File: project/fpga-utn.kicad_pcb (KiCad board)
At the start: 2 copper layers, 100 x 75 mm, 145 parts, among them J1 USB_C_Receptacle_USB2.0_16P, P1 Conector SMD 2x10, P2 Conector SMD 2x10, P3 Conector SMD 2x10, P4 Conector SMD 2x10, SW1 SW_Push, SW2 SW_Push, SW3 SW_Push, SW4 SW_Push, SW5 SW_Push, SW6 SW_Push, SW7 SW_Push, SW8 SW_Push, U1 LD1117S33TR_SOT223, U2 LD1117S12TR_SOT223, U3 USBLC6-2SC6, U4 FT2232HL, U5 M93C66, U6 ICE40HX4K-TQ144, U7 W25X40CLSN, Y1 ECS-3225MV-120-CN-TR, Y2 ECS-3225MVQ-1000-CN-TR

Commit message: pcbv1 silkscreen back connectors
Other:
- board text added: "+3V3"
- board text added: "+5V"
- board text added: "GND"
- board text added: "IOL_10A"
- board text added: "IOL_10B"
- board text added: "IOL_12A"
- board text added: "IOL_12B"
- board text added: "IOL_13A"
- board text added: "IOL_13B"
- board text added: "IOL_14A"
- board text added: "IOL_14B"
- board text added: "IOL_17A"
- board text added: "IOL_17B"
- board text added: "IOL_18A"
- board text added: "IOL_18B"
- board text added: "IOL_23A"
- board text added: "IOL_23B"
- board text added: "IOL_24A"
- board text added: "IOL_24B"
- board text added: "IOL_25A"
- board text added: "IOL_25B"
- board text added: "IOL_2A"
- board text added: "IOL_2B"
- board text added: "IOL_3A"
- board text added: "IOL_3B"
- board text added: "IOL_4A"
- board text added: "IOL_4B"
- board text added: "IOL_5A"
- board text added: "IOL_5B"
- board text added: "IOL_8A"
- board text added: "IOL_8B"
- board text added: "IOR_109"
- board text added: "IOR_110"
- board text added: "IOR_111"
- board text added: "IOR_112"
- board text added: "IOR_114"
- board text added: "IOR_115"
- board text added: "IOR_116"
- board text added: "IOR_117"
- board text added: "IOR_118"
- board text added: "IOR_119"
- board text added: "IOR_120"
- board text added: "IOR_128"
- board text added: "IOR_136"
- board text added: "IOR_137"
- board text added: "IOR_139"
- board text added: "IOR_140"
- board text added: "IOR_141"
- board text added: "IOR_144"
- board text added: "IOR_146"
- board text added: "IOR_147"
- board text added: "IOR_148"
- board text added: "IOR_152"
- board text added: "IOR_160"
- board text added: "IOR_161"
- board text added: "IOR_164"
- board text added: "IOR_165"
- board text added: "IOR_166"
- board text added: "IOR_167"

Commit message: Back silkscreen finished
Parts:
- added REF**: WEEE-Logo_4.2x6mm_SilkScreen, Symbol:WEEE-Logo_4.2x6mm_SilkScreen, B.Cu at (221.0, 145.0)
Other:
- board text added: "AZUKAR - FPGA OpenSource"
- board text added: "OSHWA UID: Pending"
- board text added: "VERSION 1.1 © 2026"
- board text added: "www.azukar.com.ar"

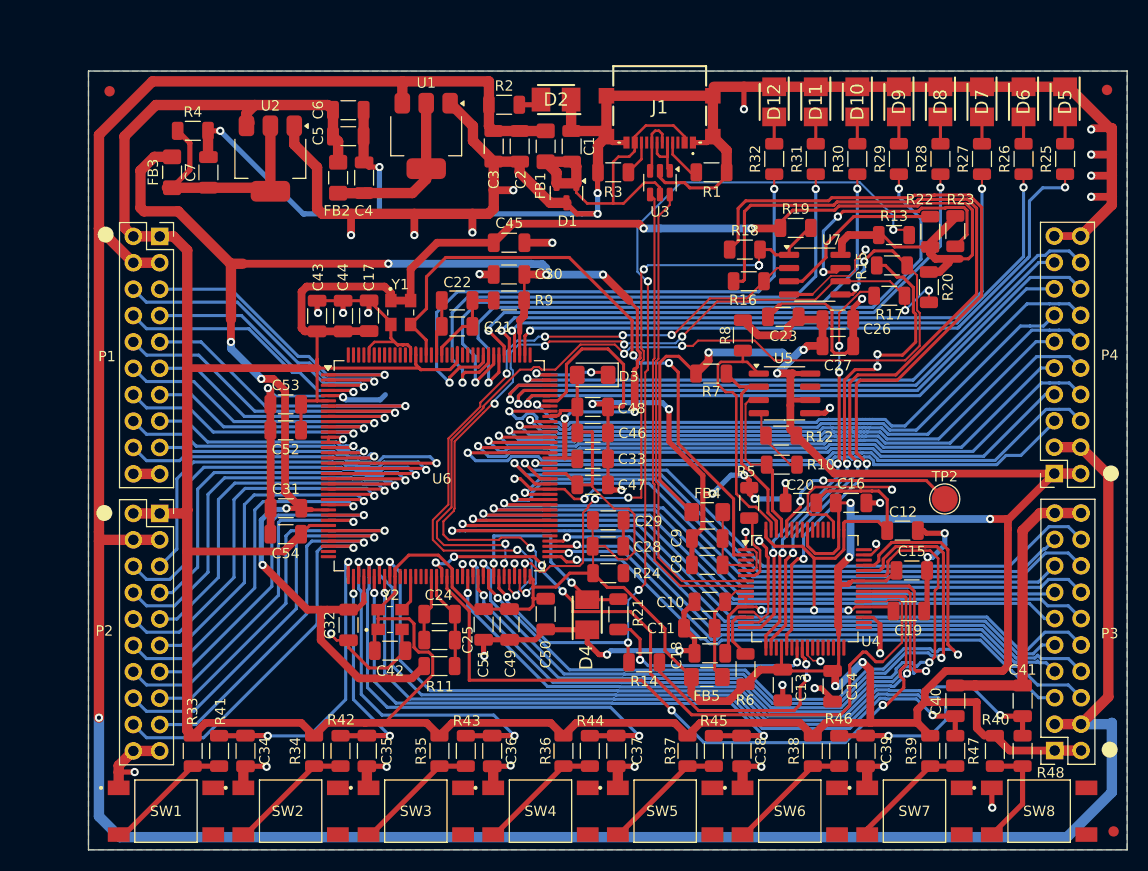
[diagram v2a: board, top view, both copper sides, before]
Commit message: pcbv1 version finalizada, correcciones de pistas, agregado logo azukar, etc
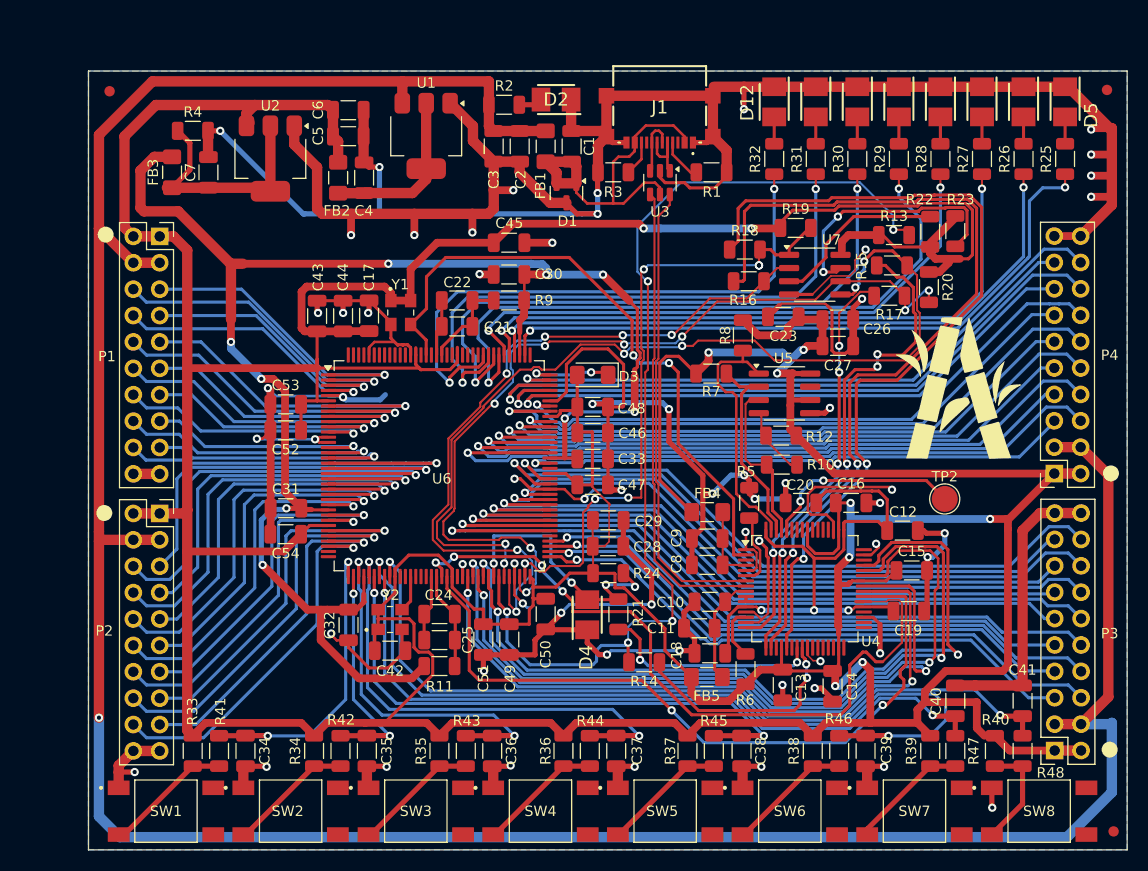
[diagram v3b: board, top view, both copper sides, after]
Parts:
- moved REF** 89.2 mm to (131.8, 145.2)
- moved C49 1.45 mm to (167.0, 129.0)
- moved C51 1.45 mm to (164.5, 129.0)
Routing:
- net GND: track 559.2 -> 592.0 mm, vias 58 -> 62
- net Net-(U6E-~{CRESET}): track 90.1 -> 99.1 mm
- net Net-(D4-A): track 20.0 -> 26.8 mm, vias 2 -> 4
- net Net-(U6E-IOB_106_SDI): track 68.1 -> 71.2 mm
- net /Perifericos/VUART_RTS: track 62.9 -> 65.4 mm
- net /Perifericos/VUART_DSR: track 74.3 -> 76.7 mm
- net /Perifericos/VUART_DCD: track 73.3 -> 75.4 mm
- net +3V3: track 669.2 -> 667.2 mm
- net /Perifericos/VUART_DTR: track 70.8 -> 72.4 mm
- net Net-(P4-IO1): track 54.8 -> 53.3 mm
- net Net-(P3-IO6): track 74.2 -> 72.8 mm
- net /Perifericos/VUART_CTS: track 68.5 -> 69.8 mm
- net Net-(P4-IO9): track 62.8 -> 62.0 mm
- net Net-(P4-IO2): track 70.9 -> 70.1 mm
- net Net-(P2-IO1): track 44.0 -> 43.1 mm
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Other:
- board text added: "AZUKAR - FPGA Tucumana"
- board text added: "BOT 1"
- board text added: "BOT 2"
- board text added: "BOT 3"
- board text added: "BOT 4"
- board text added: "BOT 5"
- board text added: "BOT 6"
- board text added: "BOT 7"
- board text added: "BOT 8"
- board text added: "IOB_56"
- board text added: "IOB_57"
- board text added: "IOB_61"
- board text added: "IOB_63"
- board text added: "IOB_64"
- board text added: "IOB_71"
- board text added: "IOB_72"
- board text added: "IOB_73"
- board text added: "IOT_168"
- board text added: "IOT_169"
- board text added: "IOT_170"
- board text added: "IOT_171"
- board text added: "IOT_172"
- board text added: "IOT_173"
- board text added: "IOT_174"
- board text added: "IOT_177"
- board text added: "LED 1"
- board text added: "LED 2"
- board text added: "LED 3"
- board text added: "LED 4"
- board text added: "LED 5"
- board text added: "LED 6"
- board text added: "LED 7"
- board text added: "LED 8"
- board text added: "ZUKAR"
- board text added: "ZUKAR - FPGA Tucumana"
- board text removed: "AZUKAR - FPGA OpenSource"

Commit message: Correccion en nombre y logo
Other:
- board text added: "AZUKAR FPGA"
- board text added: "VERSION 1.2 © 2026"
- board text removed: "AZUKAR - FPGA Tucumana"
- board text removed: "VERSION 1.1 © 2026"
- board text removed: "ZUKAR"
- board text removed: "ZUKAR - FPGA Tucumana"

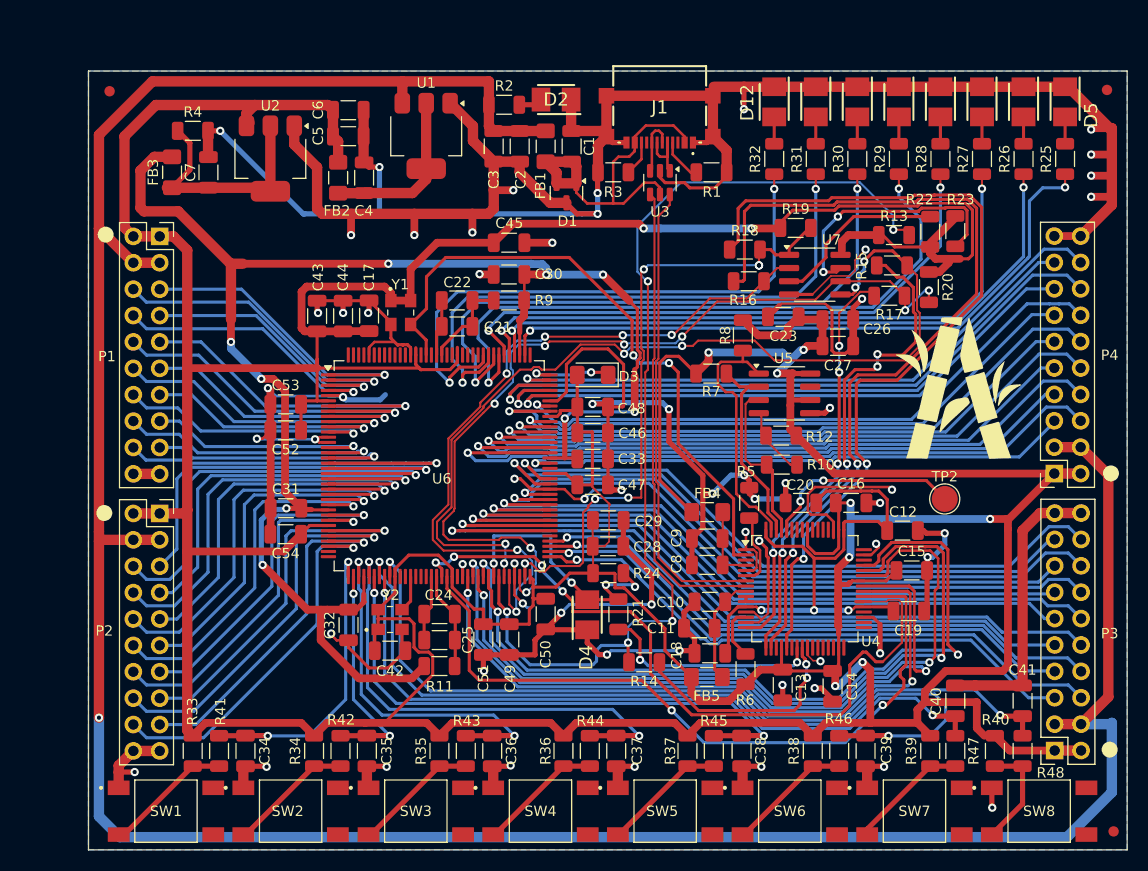
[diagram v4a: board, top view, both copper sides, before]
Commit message: Agregado de datasheets, cambio de regulador zener, ajuste de posicion de regulador, modelo 3d de oscilador
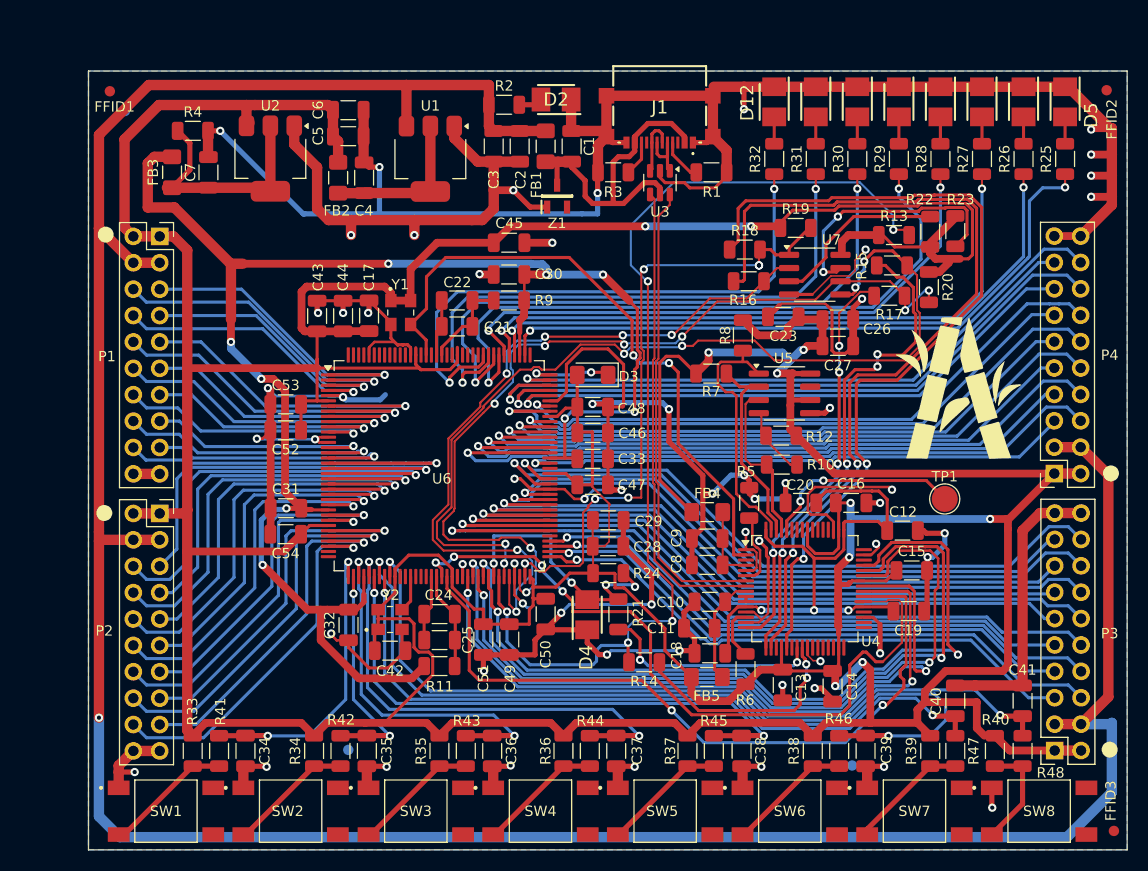
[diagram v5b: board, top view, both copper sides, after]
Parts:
- removed D1: ~, Package_TO_SOT_SMD:SOT-23
- removed FID1, FID2, FID3: Fiducial, Fiducial:Fiducial_1mm_Mask2mm
- added BFID4: Fiducial, Fiducial:Fiducial_1mm_Mask2mm, B.Cu at (130.0, 78.1)
- added BFID5: Fiducial, Fiducial:Fiducial_1mm_Mask2mm, B.Cu at (151.5, 139.6)
- added BFID6: Fiducial, Fiducial:Fiducial_1mm_Mask2mm, B.Cu at (200.0, 141.1)
- added FFID1: Fiducial, Fiducial:Fiducial_1mm_Mask2mm, F.Cu at (128.6, 76.2)
- added FFID2: Fiducial, Fiducial:Fiducial_1mm_Mask2mm, F.Cu at (224.5, 76.1)
- added FFID3: Fiducial, Fiducial:Fiducial_1mm_Mask2mm, F.Cu at (225.2, 147.4)
- added Z1: MMBZ5231BLT3G, MMBZ5231BLT3G:SOT96P237X111-3N, F.Cu at (171.6, 86.3)
- C34, C35, C36, C37, C38, C39, C40, C41: value 10uF -> 10u
- C43, C46, C49, C52: value 1uF -> 1u
- D10, D11, D12, D9: value LED Red -> LED Green
- D2: value LED Green -> LED Red
- R15, R16, R17, R18, R25, R26, R27, R28, R29, R30, R31, R32: value R -> 220
- R21: value 220R -> 220
- U1: value LD1117S33TR_SOT223 -> LD1117S33CTR
- U2: value LD1117S12TR_SOT223 -> LD1117S12CTR
- moved U1 2.24 mm to (159.4, 82.7)
- renumbered TP2 to TP1
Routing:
- net GND: track 592.0 -> 581.5 mm, vias 62 -> 60
- net Net-(U1-VO): track 16.4 -> 13.5 mm
- net Net-(U3-VBUS): track 34.4 -> 32.2 mm
- net +5V: track 274.2 -> 275.6 mm
- net +1V2: track 162.0 -> 160.9 mm
- net +3V3: track 667.2 -> 666.3 mm
- net Net-(U6E-~{CRESET}): track 99.1 -> 99.8 mm

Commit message: Correcion de errores ERC y DRC, avisos ERC y DRC, correccion de huellas, silksreens pisando soldermask, etc
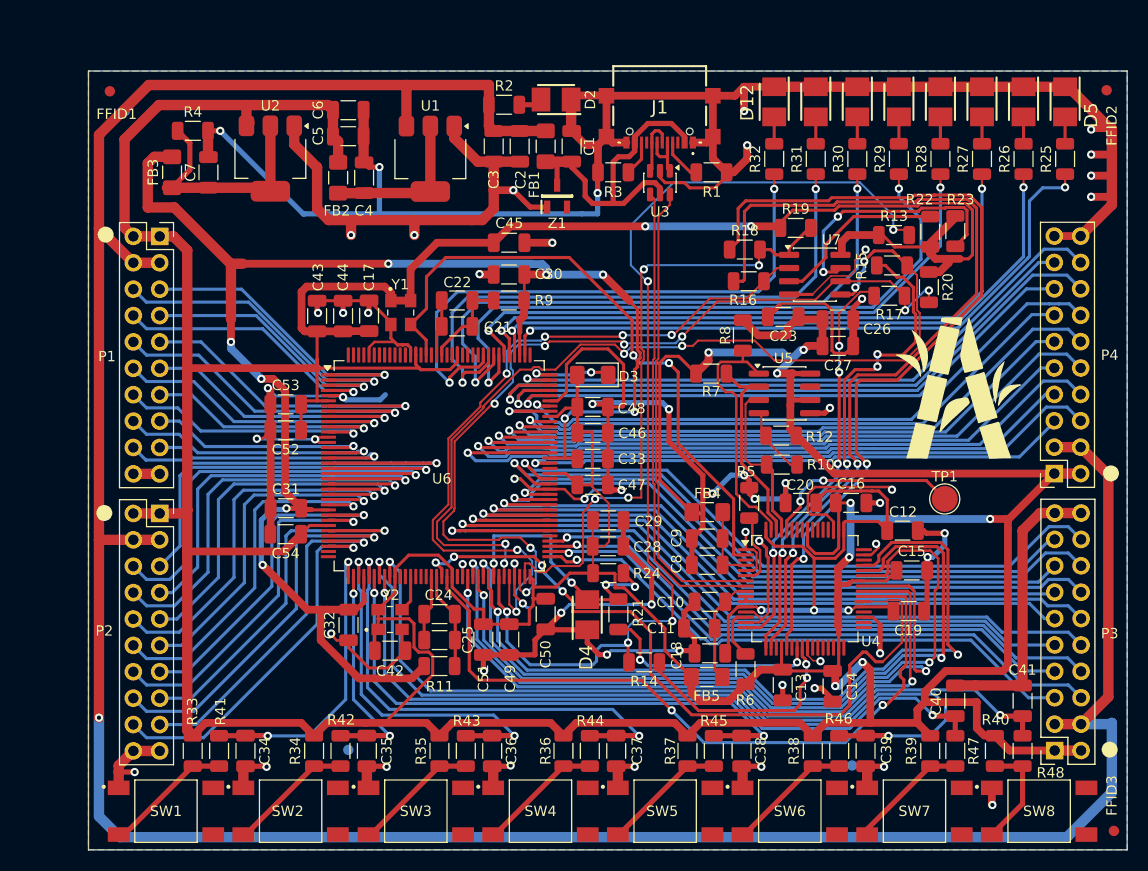
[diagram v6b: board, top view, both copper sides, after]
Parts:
- P1, P2, P3, P4: value Conector SMD 2x10 -> Conector 2x10
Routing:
- net GND: track 581.5 -> 587.3 mm, vias 60 -> 61
- net +1V2: track 160.9 -> 160.0 mm
- net Net-(U6E-IOB_108_SS): vias 6 -> 4

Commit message: Pistas, pads, soldermask y silkscreen corregidas para pasar analisis DMF de jlcpcb.
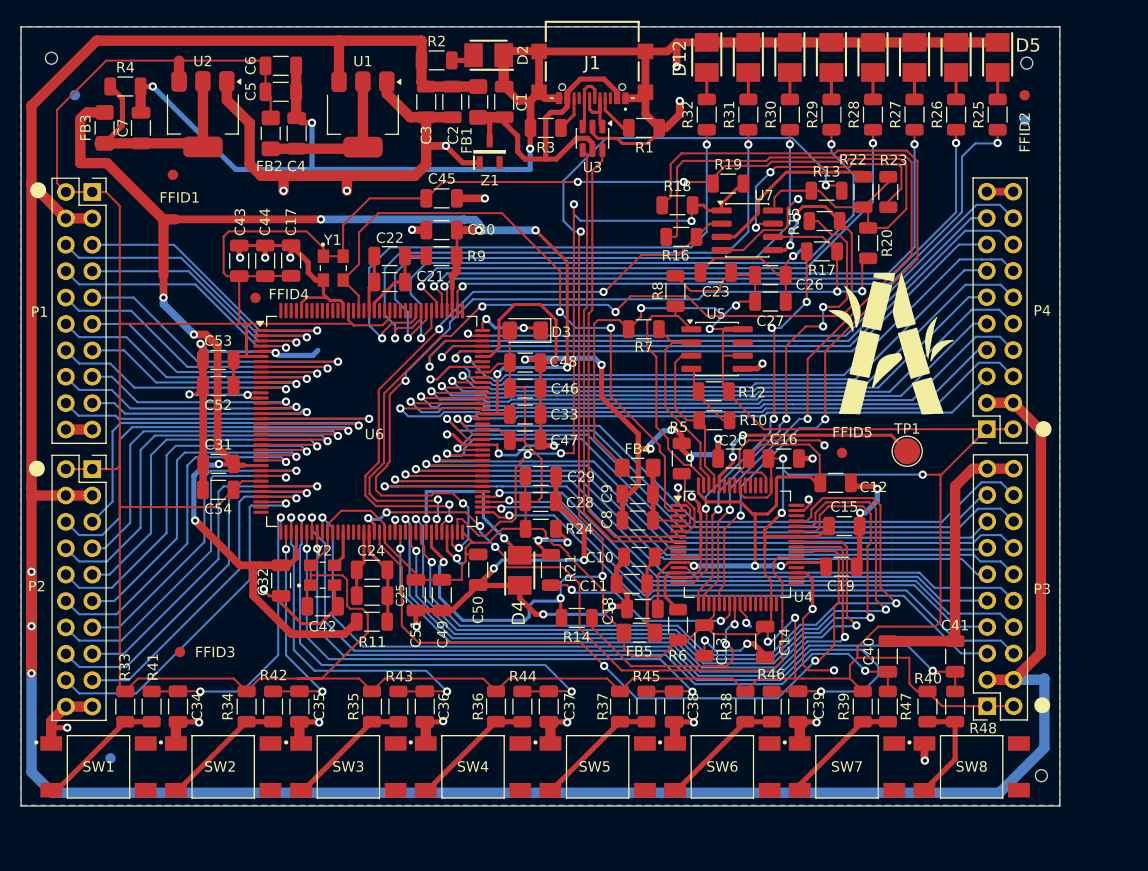
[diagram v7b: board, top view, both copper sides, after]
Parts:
- removed BFID4: Fiducial, Fiducial:Fiducial_1mm_Mask2mm
- added BFID6: Fiducial, Fiducial:Fiducial_1mm_Mask2mm, B.Cu at (216.6, 79.0)
- added FFID4: Fiducial, Fiducial:Fiducial_1mm_Mask2mm, F.Cu at (142.6, 96.1)
- added FFID5: Fiducial, Fiducial:Fiducial_1mm_Mask2mm, F.Cu at (199.0, 111.0)
- added TH1: MountingHole, MountingHole:ToolingHole_1.152mm, F.Cu at (122.9, 73.0)
- added TH2: MountingHole, MountingHole:ToolingHole_1.152mm, F.Cu at (216.8, 73.5)
- added TH3: MountingHole, MountingHole:ToolingHole_1.152mm, F.Cu at (218.2, 142.1)
- moved REF** 103.2 mm to (211.6, 79.8)
- moved FFID3 91.5 mm to (135.3, 130.2)
- moved BFID8 71.4 mm to (128.6, 140.4)
- moved BFID7 68.3 mm to (125.2, 76.6)
- moved FFID1 10.1 mm to (134.6, 84.2)
- moved C17 9.19 mm to (146.0, 92.5)
- moved C43 9.19 mm to (141.0, 92.5)
- moved C44 9.19 mm to (143.5, 92.5)
- moved C13 8.67 mm to (185.8, 129.1)
- moved C10 8.05 mm to (179.5, 121.0)
- moved C8 7.94 mm to (179.4, 117.5)
- moved C9 7.94 mm to (179.4, 115.0)
- moved FB4 7.94 mm to (179.4, 112.4)
- moved C12 7.91 mm to (198.4, 113.9)
- moved FFID2 7.90 mm to (216.6, 76.6)
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- renumbered BFID5 to BFID7, BFID6 to BFID8
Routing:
- net GND: track 587.3 -> 572.9 mm, vias 61 -> 57
- net Net-(U6E-IOB_106_SDI): track 71.2 -> 62.3 mm, vias 6 -> 4
- net +5V: track 275.5 -> 284.4 mm, vias 1 -> 3
- net Net-(U6E-IOB_107_SCK): track 84.0 -> 91.0 mm, vias 8 -> 5
- net /Perifericos/VUART_Rx: track 70.8 -> 64.1 mm
- net Net-(P4-IO13): track 62.9 -> 66.8 mm
- net Net-(U6E-IOB_108_SS): track 60.3 -> 63.9 mm
- net Net-(P4-IO9): track 62.0 -> 65.2 mm
- net Net-(U4-~{PWREN}): track 19.2 -> 22.2 mm
- net /Memorias y PLL/Flash_DO: track 84.1 -> 82.4 mm
- net Net-(P4-IO14): track 61.3 -> 59.8 mm
- net Net-(D3-K): track 8.29 -> 6.94 mm
- net /Memorias y PLL/Flash_DONE: track 21.4 -> 20.0 mm
- net /Memorias y PLL/Flash_CS: track 82.3 -> 81.0 mm
- net /Memorias y PLL/EEPROM_CLK: track 20.1 -> 21.2 mm
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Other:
- board text added: "VERSION 1.3 © 2026"
- board text removed: "VERSION 1.2 © 2026"
